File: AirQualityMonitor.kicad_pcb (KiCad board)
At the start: 4 copper layers, 72.3 x 62 mm, 177 parts, among them J1 USB_C_Receptacle_USB2.0_16P, J10 FH34SRJ-24S-0.5SH_99_E2417KS0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, J2 TC2050, J3 SM05B-GHS-TB, J4 Header, J5 BM02B-ACHSS-GAN-ETF, J6 SM04B-GHS-TB, J7 SM04B-GHS-TB, J8 SM06B-GHS-TB, J9 SM06B-GHS-TB, Q1 RV2C010UNT2L, Q2 RUM001L02T2CL, Q3 Si1308EDL, U1 TLV70033DDCR, U10 SGP41-D-R4, U11 PCA9306D, U12 SRV05-4, U13 BME690, U14 TXU0104PWR, U15 SN74LXC1T45DCKR, U16 TCK107AF,LF, U2 TLV70036DDCR, U3 USBLC6-2SC6, U4 TPS2553DDBVR, U5 nRF5340-QKxx, U6 MX25R3235FM1IH0-TR, U7 TCK107AF,LF, U8 NRF7001-QFAA-R, U9 BGS12WN6E6327, Y1 32M, Y2 32k768, Y3 Crystal_GND24

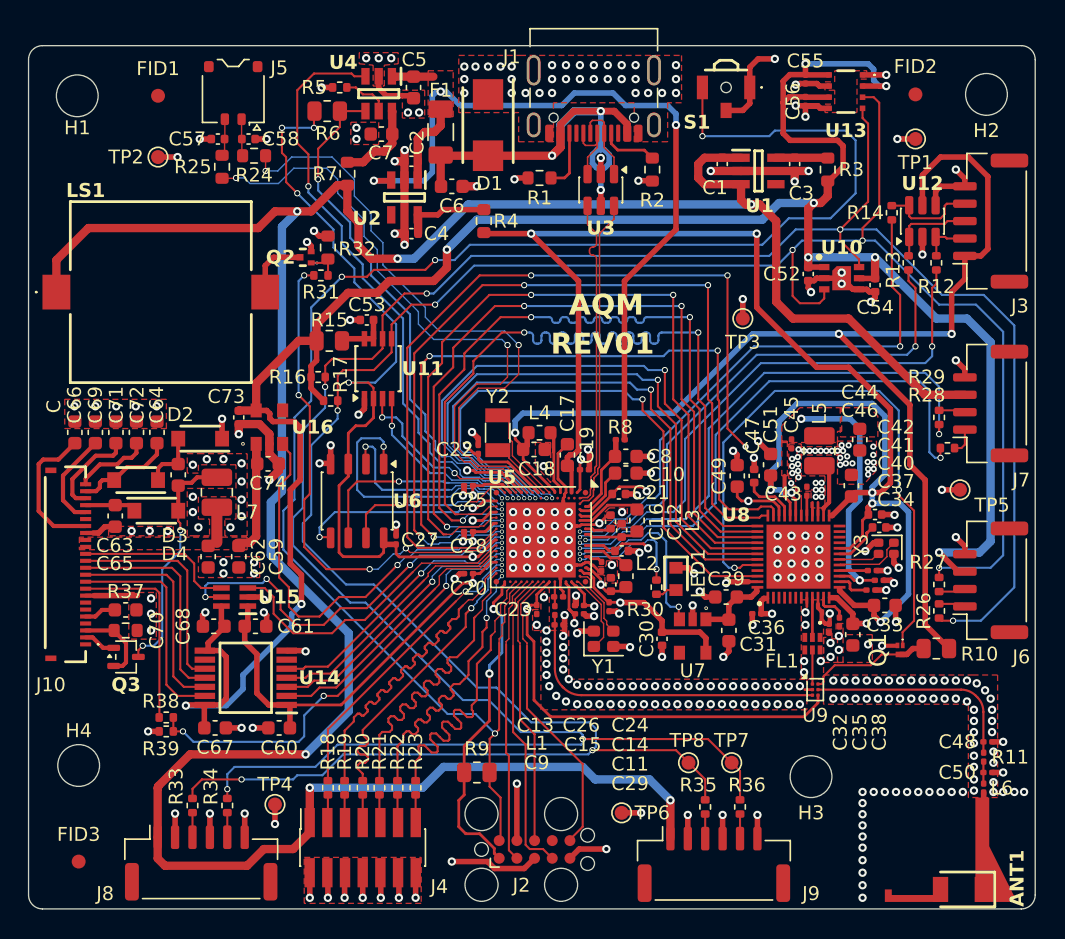
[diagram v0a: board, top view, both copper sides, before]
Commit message: Use a different LED with better forward voltage
Change the main MCU LED to a one with better forward voltage.
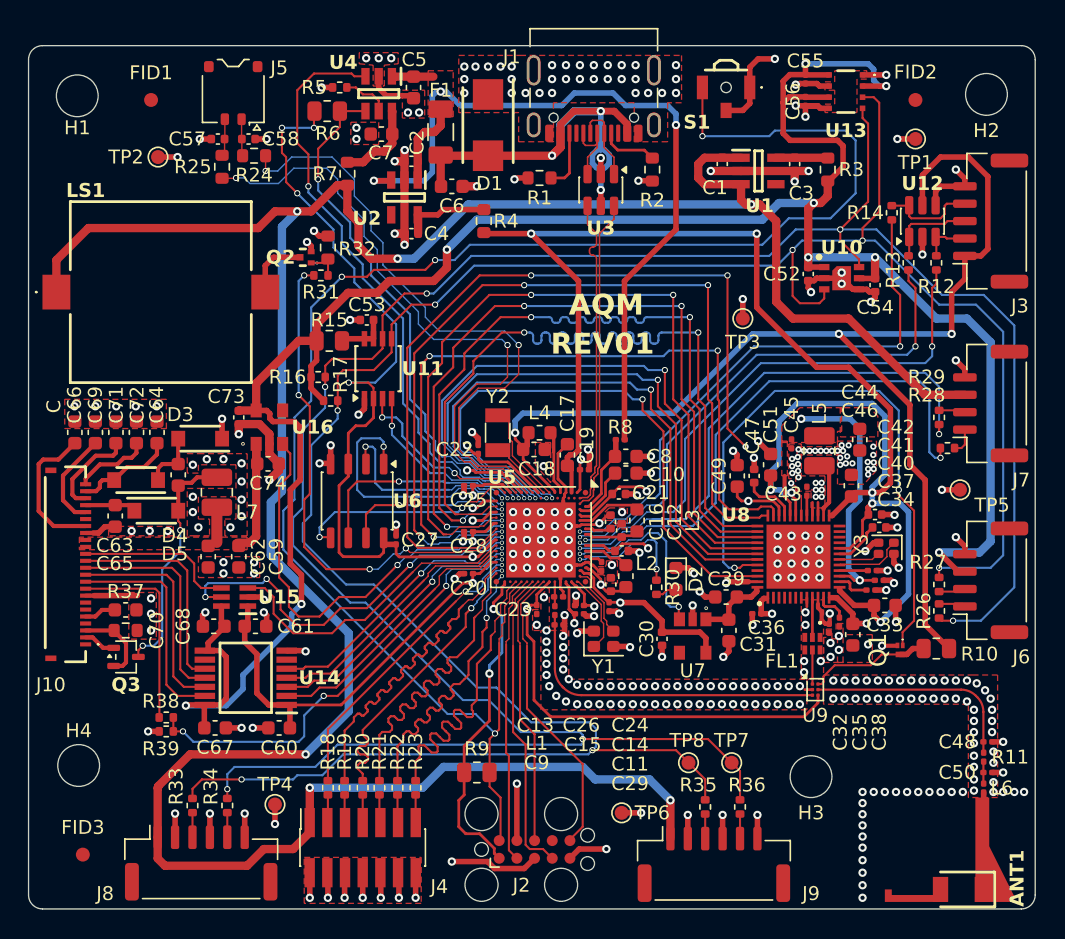
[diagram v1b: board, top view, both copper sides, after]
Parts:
- D2: renamed from LED1; value SML-D12U1WT86 -> APHD1608LSURCK; footprint SML-D12U1WT86:LEDC1608X65N -> LED_SMD:LED_0603_1608Metric
- R30: value 1.5k -> 50
- moved FID3 0.58 mm to (103.9, 96.1)
- moved FID1 0.58 mm to (108.8, 41.9)
- moved FID2 0.40 mm to (163.7, 41.9)
- renumbered D2 to D3, D3 to D4, D4 to D5
